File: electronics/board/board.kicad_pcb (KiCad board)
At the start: 2 copper layers, 61 parts, among them J1 Conn_02x05_Odd_Even, J2 USB_A, J3 Micro_SD_Card_Det_Hirose_DM3AT, SW1 SW_Push, U1 JW5211, U2 JW5211, U3 JW5211, U4 F1C100s, U5 SST26VF080A-104I/SN, U6 USBLC6-2SC6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

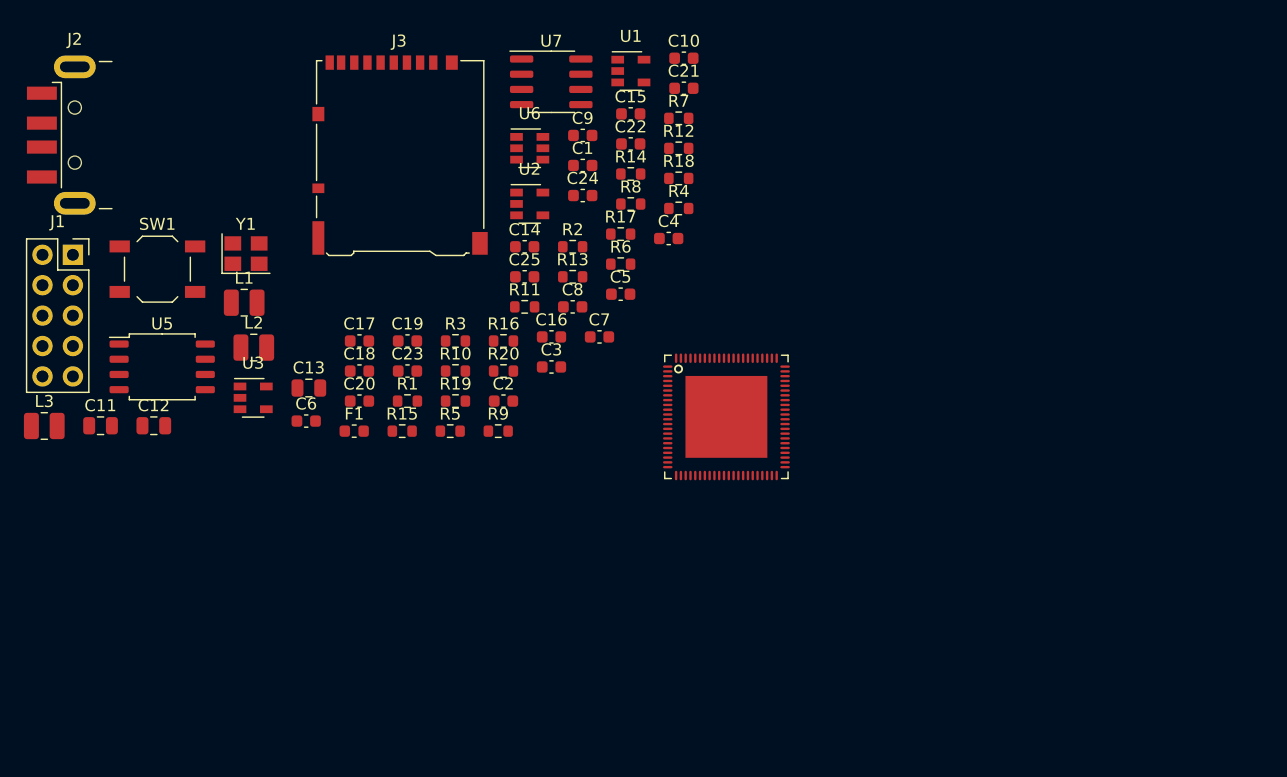
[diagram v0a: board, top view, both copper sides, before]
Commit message: Arranged the parts.
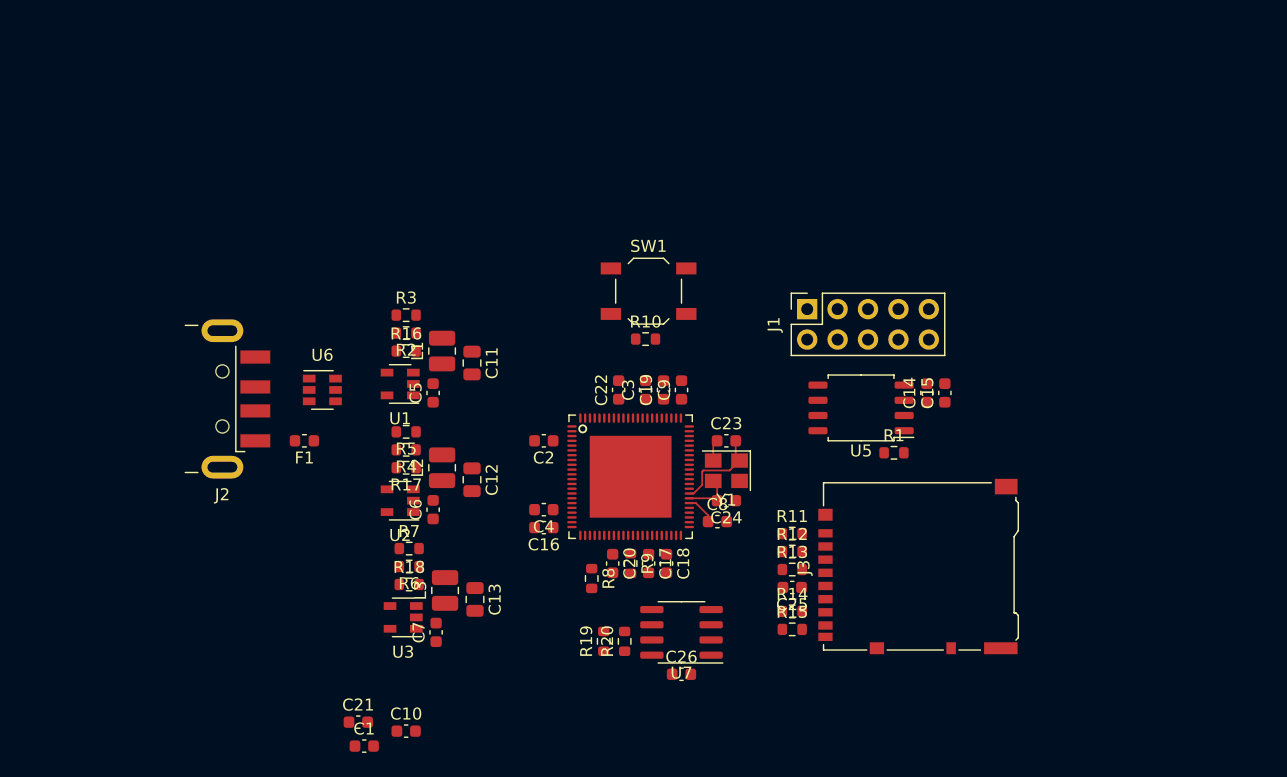
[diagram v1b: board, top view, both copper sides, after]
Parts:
- added C26: 100nF, Capacitor_SMD:C_0603_1608Metric, F.Cu at (142.2, 138.5)
- moved J1 61.5 mm to (152.8, 108.0), turned to 90 degrees
- moved C10 60.8 mm to (119.2, 143.2)
- moved C21 59.5 mm to (115.2, 142.5)
- moved U5 58.5 mm to (157.2, 116.2), turned to 180 degrees
- moved J3 55.3 mm to (162.0, 129.5), turned to 90 degrees
- moved C1 51.8 mm to (115.8, 144.5)
- moved U7 47.3 mm to (142.2, 135.0), turned to 180 degrees
- moved Y1 44.0 mm to (146.0, 121.5), turned to 180 degrees
- moved R7 42.4 mm to (119.5, 128.0)
- moved SW1 41.1 mm to (139.5, 106.5)
- moved R1 40.9 mm to (160.0, 120.0)
- moved R18 40.7 mm to (119.5, 131.0)
- moved R14 39.0 mm to (151.5, 133.2)
- moved R15 36.5 mm to (151.5, 134.8)
- moved L3 36.2 mm to (122.5, 131.5), turned to 90 degrees
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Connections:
- net Net-(R2-Pad2) renamed /3v3_FB
- net Net-(R4-Pad2) renamed /2v5_FB
- net Net-(R6-Pad2) renamed /1v1_FB
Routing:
- net Net-(C23-Pad2): track 0.00 -> 7.78 mm
- net Net-(C24-Pad2): track 0.00 -> 4.19 mm
- net +3V3: track 0.00 -> 2.52 mm
- net GND: track 0.00 -> 1.78 mm
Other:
- copper layers 2 -> 4
- net class Default: clearance 0.2 -> 0.15; trace_width 0.25 -> 0.15; via_dia 0.8 -> 0.4; via_drill 0.4 -> 0.2
- net class Outer_Small added: clearance 0.1, trace_width 0.1, via_dia 0.4, via_drill 0.2
- net class Power added: clearance 0.2, trace_width 1, via_dia 0.8, via_drill 0.6
- rule trace_clearance: 0.2 -> 0.15
- rule trace_min: 0.2 -> 0.09
- rule via_min_drill: 0.3 -> 0.2

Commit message: Dropped in the 3d models and outlined the board.
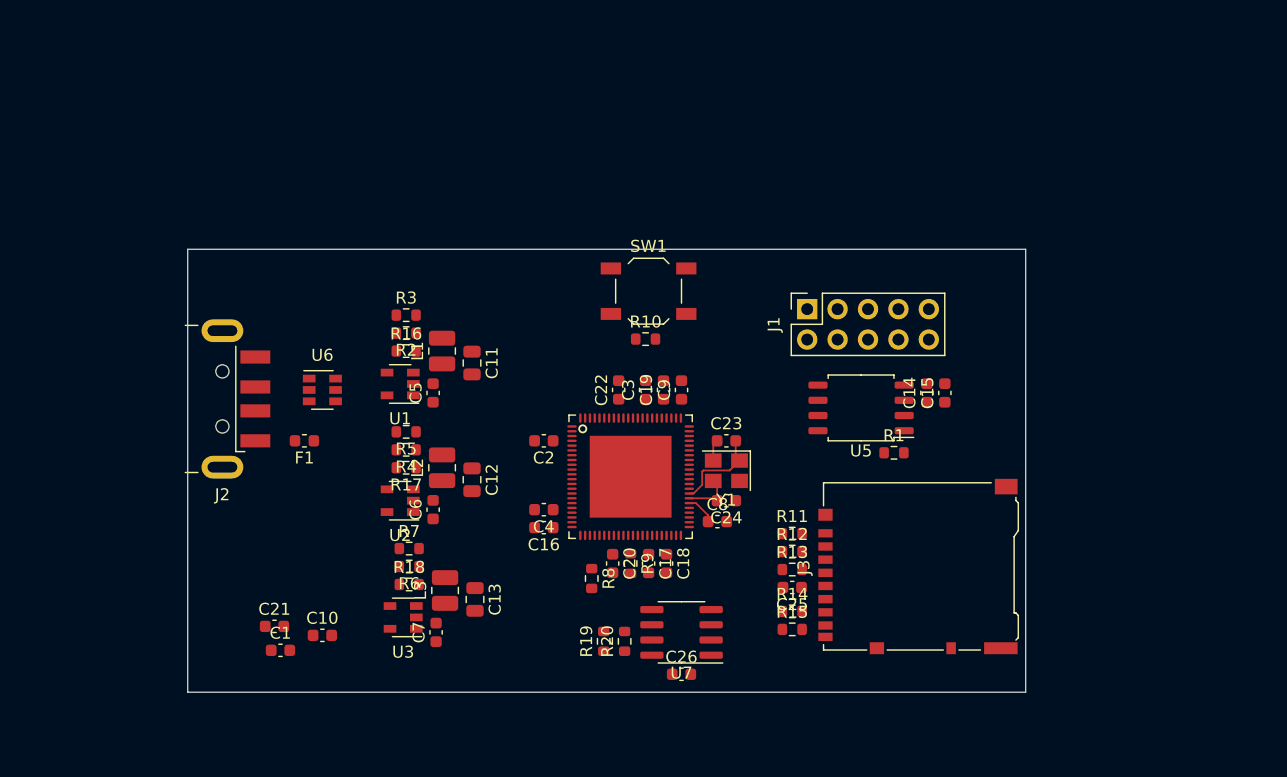
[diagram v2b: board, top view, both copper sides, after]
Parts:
- moved C1 10.6 mm to (108.8, 136.5)
- moved C10 10.6 mm to (112.2, 135.2)
- moved C21 10.6 mm to (108.2, 134.5)
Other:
- board outline added: 70 x 37 mm

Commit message: Started the main routing.
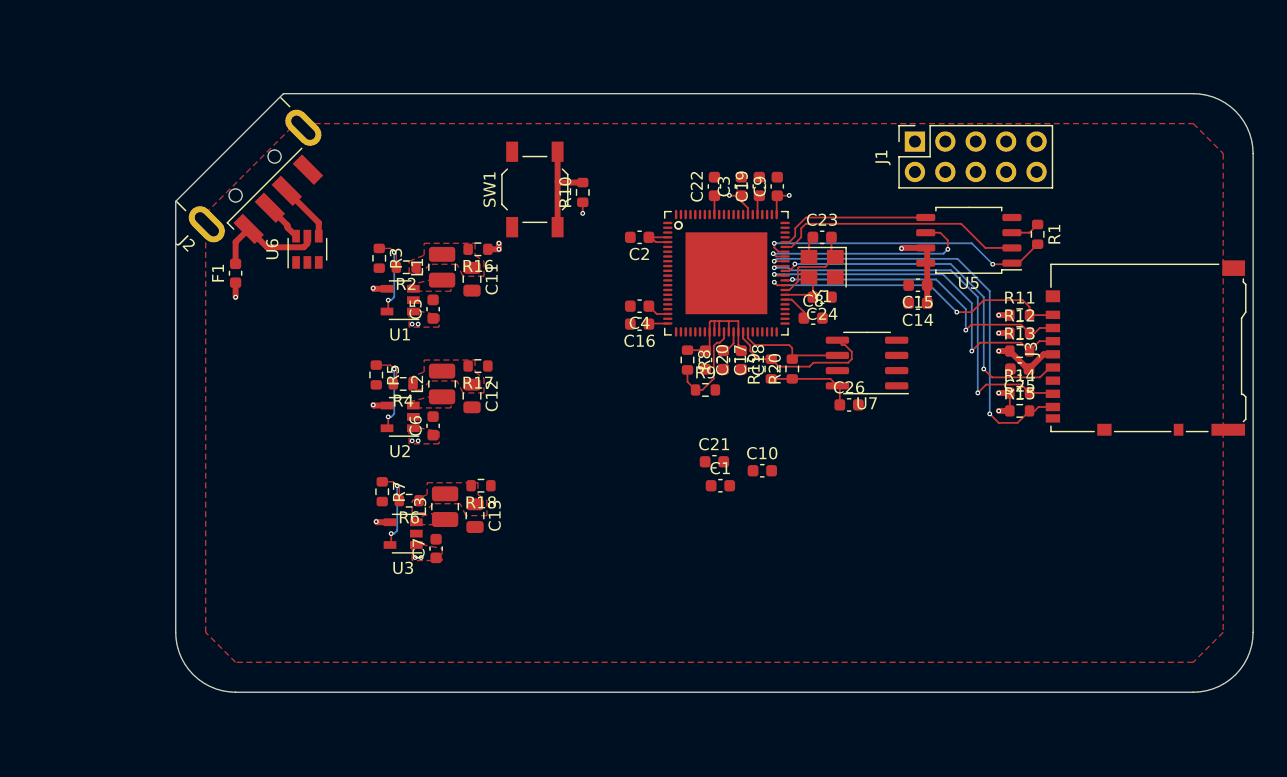
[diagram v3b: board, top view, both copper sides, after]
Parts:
- moved C1 39.2 mm to (145.5, 122.8)
- moved C10 39.2 mm to (149.0, 121.5)
- moved C21 39.2 mm to (145.0, 120.8)
- moved U7 27.3 mm to (157.8, 112.5)
- moved R19 26.7 mm to (149.8, 113.0)
- moved R20 26.7 mm to (151.5, 113.0)
- moved C26 26.5 mm to (156.2, 116.0)
- moved C25 26.3 mm to (170.5, 113.0)
- moved J3 26.3 mm to (181.0, 111.2)
- moved R11 26.3 mm to (170.5, 108.5)
- moved R12 26.3 mm to (170.5, 110.0)
- moved R13 26.3 mm to (170.5, 111.5)
- moved R14 26.3 mm to (170.5, 115.0)
- moved R15 26.3 mm to (170.5, 116.5)
- moved J2 24.0 mm to (101.8, 92.0), turned to 135 degrees
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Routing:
- net +3V3: track 2.52 -> 69.9 mm, vias 0 -> 11
- net /SDC0_D1: track 0.00 -> 36.5 mm, vias 0 -> 2
- net /SDC0_D0: track 0.00 -> 33.9 mm, vias 0 -> 2
- net /SDC0_CLK: track 0.00 -> 30.5 mm, vias 0 -> 2
- net /SDC0_CMD: track 0.00 -> 30.1 mm, vias 0 -> 2
- net /SDC0_D2: track 0.00 -> 26.7 mm, vias 0 -> 2
- net /SDC0_D3: track 0.00 -> 25.8 mm, vias 0 -> 2
- net /SPI_CS: track 0.00 -> 24.8 mm, vias 0 -> 2
- net /SPI_MISO: track 0.00 -> 21.0 mm
- net /SPI_CK: track 0.00 -> 18.7 mm, vias 0 -> 2
- net /TWI0_SDA: track 0.00 -> 14.1 mm
- net +2V5: track 0.00 -> 13.3 mm
- net /SPI_MOSI: track 0.00 -> 13.0 mm
- net VBUS: track 0.00 -> 9.66 mm
- net /TWI0_SCK: track 0.00 -> 9.40 mm
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- added copper zone on In1.Cu, net +3V3
- added copper zone on F.Cu, net +5V
- added copper zone on In1.Cu, net +5V
- added copper zone on F.Cu, net GND
- added copper zone on F.Cu, net Net-(C11-Pad1)
- added copper zone on F.Cu, net Net-(C12-Pad1)
- added copper zone on F.Cu, net Net-(C13-Pad1)
- added copper zone on F.Cu, net Net-(L1-Pad1)
- added copper zone on F.Cu, net Net-(L2-Pad1)
- added copper zone on F.Cu, net Net-(L3-Pad1)
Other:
- board size 70 x 37 mm -> 90 x 50 mm

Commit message: Nearly finished up all the layout, power distrobution done. Just a couple more nets to connect up and silk.
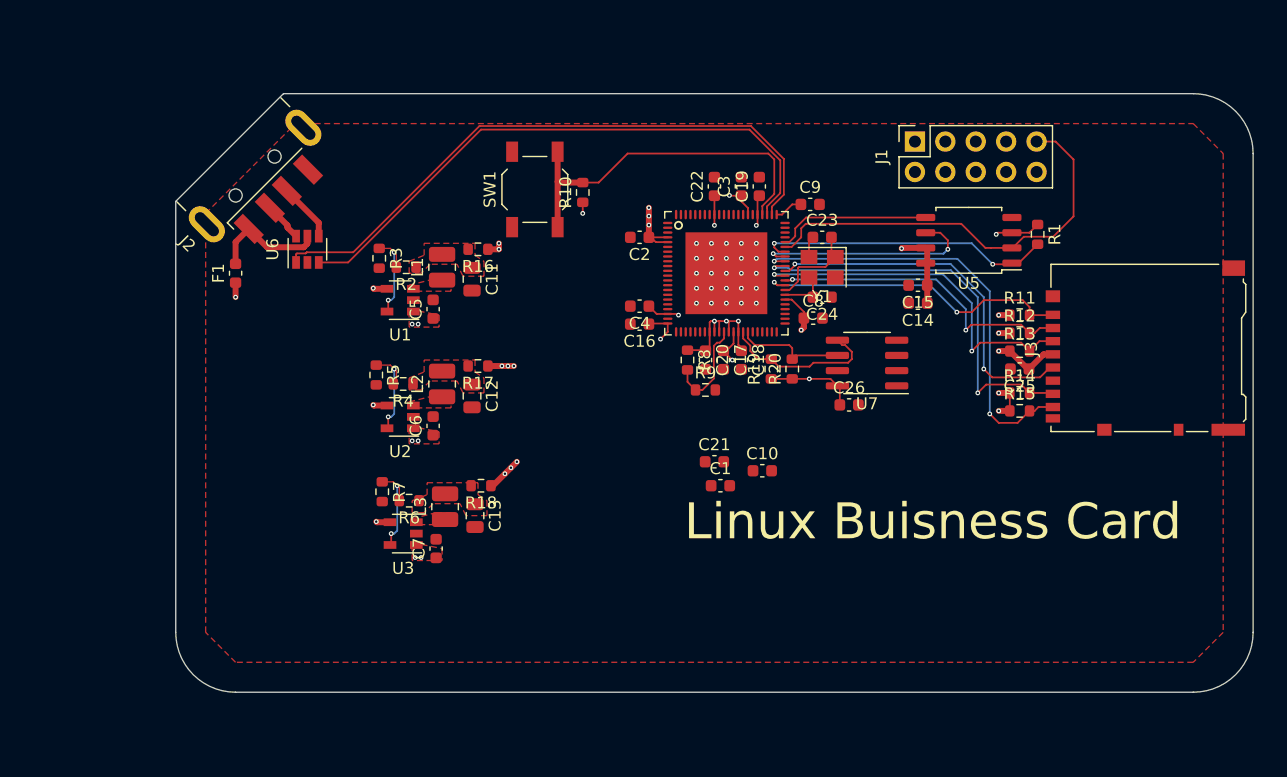
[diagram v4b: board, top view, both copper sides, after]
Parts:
- moved C9 3.13 mm to (153.0, 99.2), turned to 0 degrees
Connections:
- net /USB_DM renamed /USB_N
- net /USB_DP renamed /USB_P
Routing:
- net +5V: track 4.72 -> 60.0 mm
- net /USB_N: track 0.00 -> 52.1 mm
- net /USB_P: track 0.00 -> 49.2 mm
- net /!RST: track 8.33 -> 30.6 mm
- net +3V3: track 69.9 -> 48.5 mm, vias 11 -> 17
- net /SPI_MISO: track 21.0 -> 35.7 mm
- net +1V1: track 5.06 -> 11.6 mm, vias 0 -> 6
- net +2V5: track 13.3 -> 16.4 mm, vias 0 -> 7
- net GND: vias 0 -> 25
- added copper zone on In1.Cu, net +1V1
- added copper zone on In1.Cu, net +2V5
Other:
- board text added: "Linux Buisness Card"

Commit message: Layout finished, added some images.
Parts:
- removed C1, C10, C21: 100nF, Capacitor_SMD:C_0603_1608Metric
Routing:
- net /UART_TX: track 0.00 -> 27.6 mm, vias 0 -> 1
- net /!RST: track 30.6 -> 55.3 mm, vias 0 -> 2
- net /UART_RX: track 0.00 -> 22.8 mm, vias 0 -> 1
- net /SPI_CS: track 24.8 -> 36.0 mm, vias 2 -> 4
- net /SPI_MOSI: track 13.0 -> 22.4 mm
- net /SPI_CK: track 18.7 -> 27.7 mm, vias 2 -> 3
- added copper zone on B.Cu, net GND
- added copper zone on In2.Cu, net GND
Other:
- board text added: "Joel Raider"

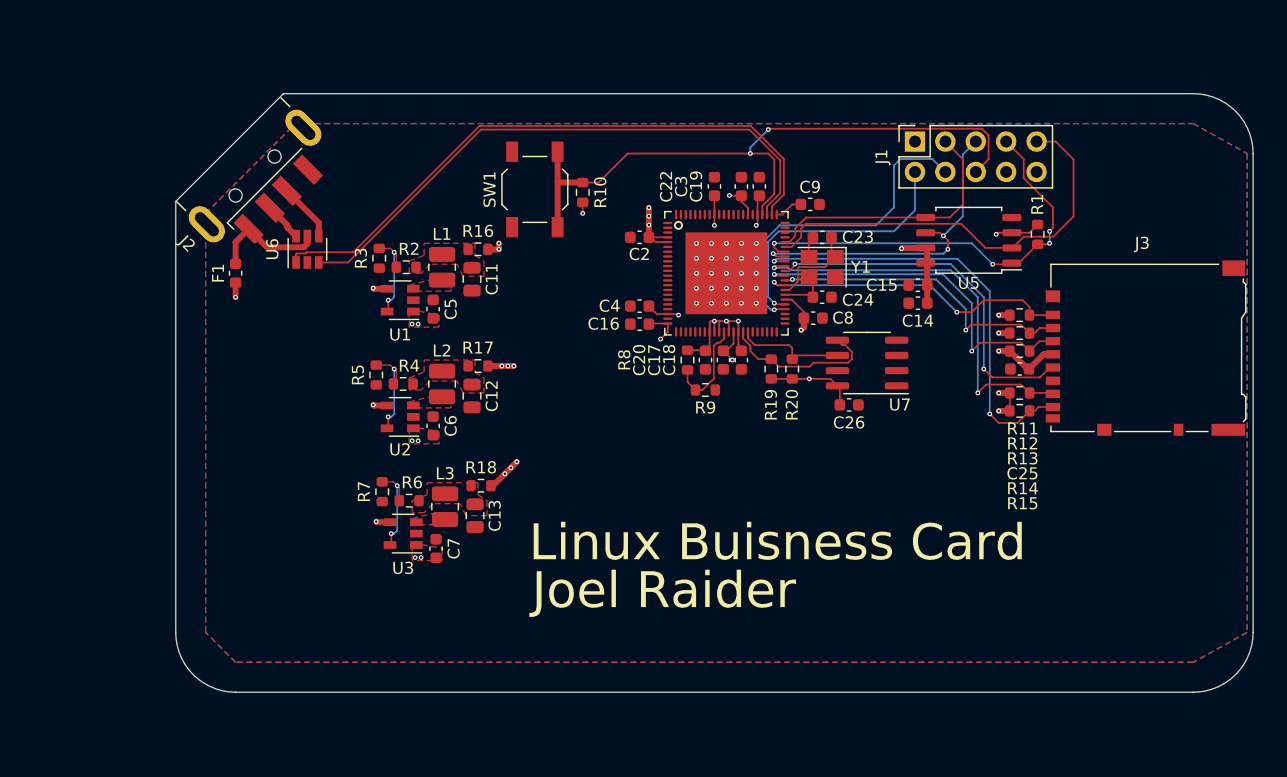
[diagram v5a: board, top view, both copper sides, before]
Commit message: Filled in the rest of the part numbers, generated a bom.
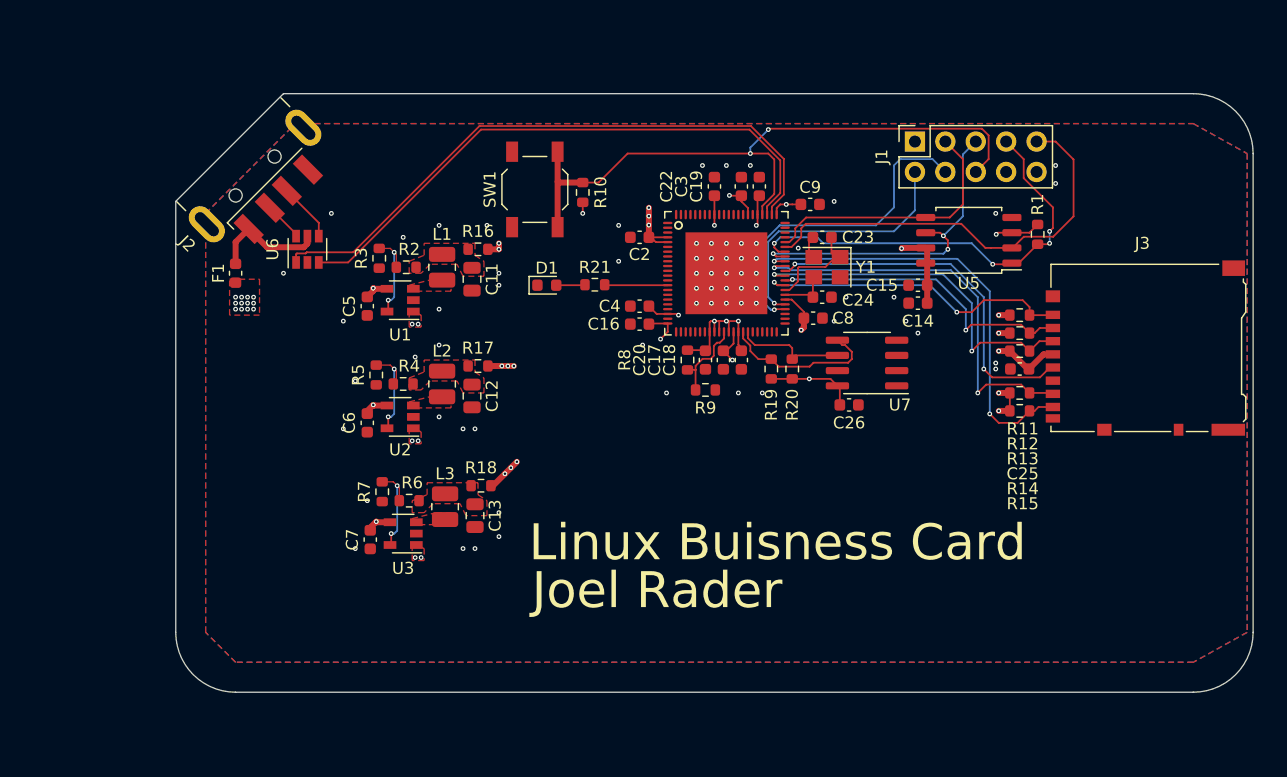
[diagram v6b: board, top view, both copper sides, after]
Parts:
- added D1: LED, LED_SMD:LED_0603_1608Metric, F.Cu at (131.0, 106.0)
- added R21: 4.7k, Resistor_SMD:R_0603_1608Metric, F.Cu at (135.0, 106.0)
- moved C7 5.55 mm to (116.2, 127.2), turned to 270 degrees
- moved C5 5.51 mm to (116.0, 107.8), turned to 270 degrees
- moved C6 5.51 mm to (116.0, 117.5), turned to 270 degrees
- moved Y1 0.40 mm to (154.4, 104.5)
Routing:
- net Net-(R21-Pad1): track 0.00 -> 5.28 mm
- net Net-(D1-Pad2): track 0.00 -> 2.41 mm
- net +5V: track 60.0 -> 61.5 mm, vias 10 -> 21
- net Net-(R8-Pad2): track 8.26 -> 7.04 mm
- net +3V3: track 48.5 -> 48.9 mm, vias 17 -> 18
- net GND: vias 25 -> 68
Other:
- board text added: "Joel Rader"
- board text removed: "Joel Raider"
